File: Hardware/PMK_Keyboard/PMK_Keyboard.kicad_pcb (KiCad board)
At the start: 2 copper layers, 172 x 152 mm, 52 parts, among them IC1 SN74HC165PWR, IC2 SN74HC165PWR, IC3 SN74HC165PWR, IC4 SN74HC165PWR, IC5 SN74HC165PWR, IC7 ESP32-S2FH4, SW1 SW_Push, SW10 SW_Push, SW11 SW_Push, SW12 SW_Push, SW13 SW_Push, SW14 SW_Push, SW15 SW_Push, SW16 SW_Push, SW17 SW_Push, SW18 SW_Push, SW19 SW_Push, SW2 SW_Push, SW20 SW_Push, SW21 SW_Push, SW22 SW_Push, SW23 SW_Push, SW24 SW_Push, SW25 SW_Push, SW26 SW_Push, SW27 SW_Push, SW28 SW_Push, SW29 SW_Push, SW3 SW_Push, SW30 SW_Push, SW31 SW_Push, SW32 SW_Push, SW33 SW_Push, SW34 SW_Push, SW35 SW_Push, SW36 SW_Push, SW37 SW_Push, SW38 SW_Push, SW39 SW_Push, SW4 SW_Push, SW40 SW_Push, SW5 SW_Push, SW6 SW_Push, SW7 SW_Push, SW8 SW_Push, SW9 SW_Push

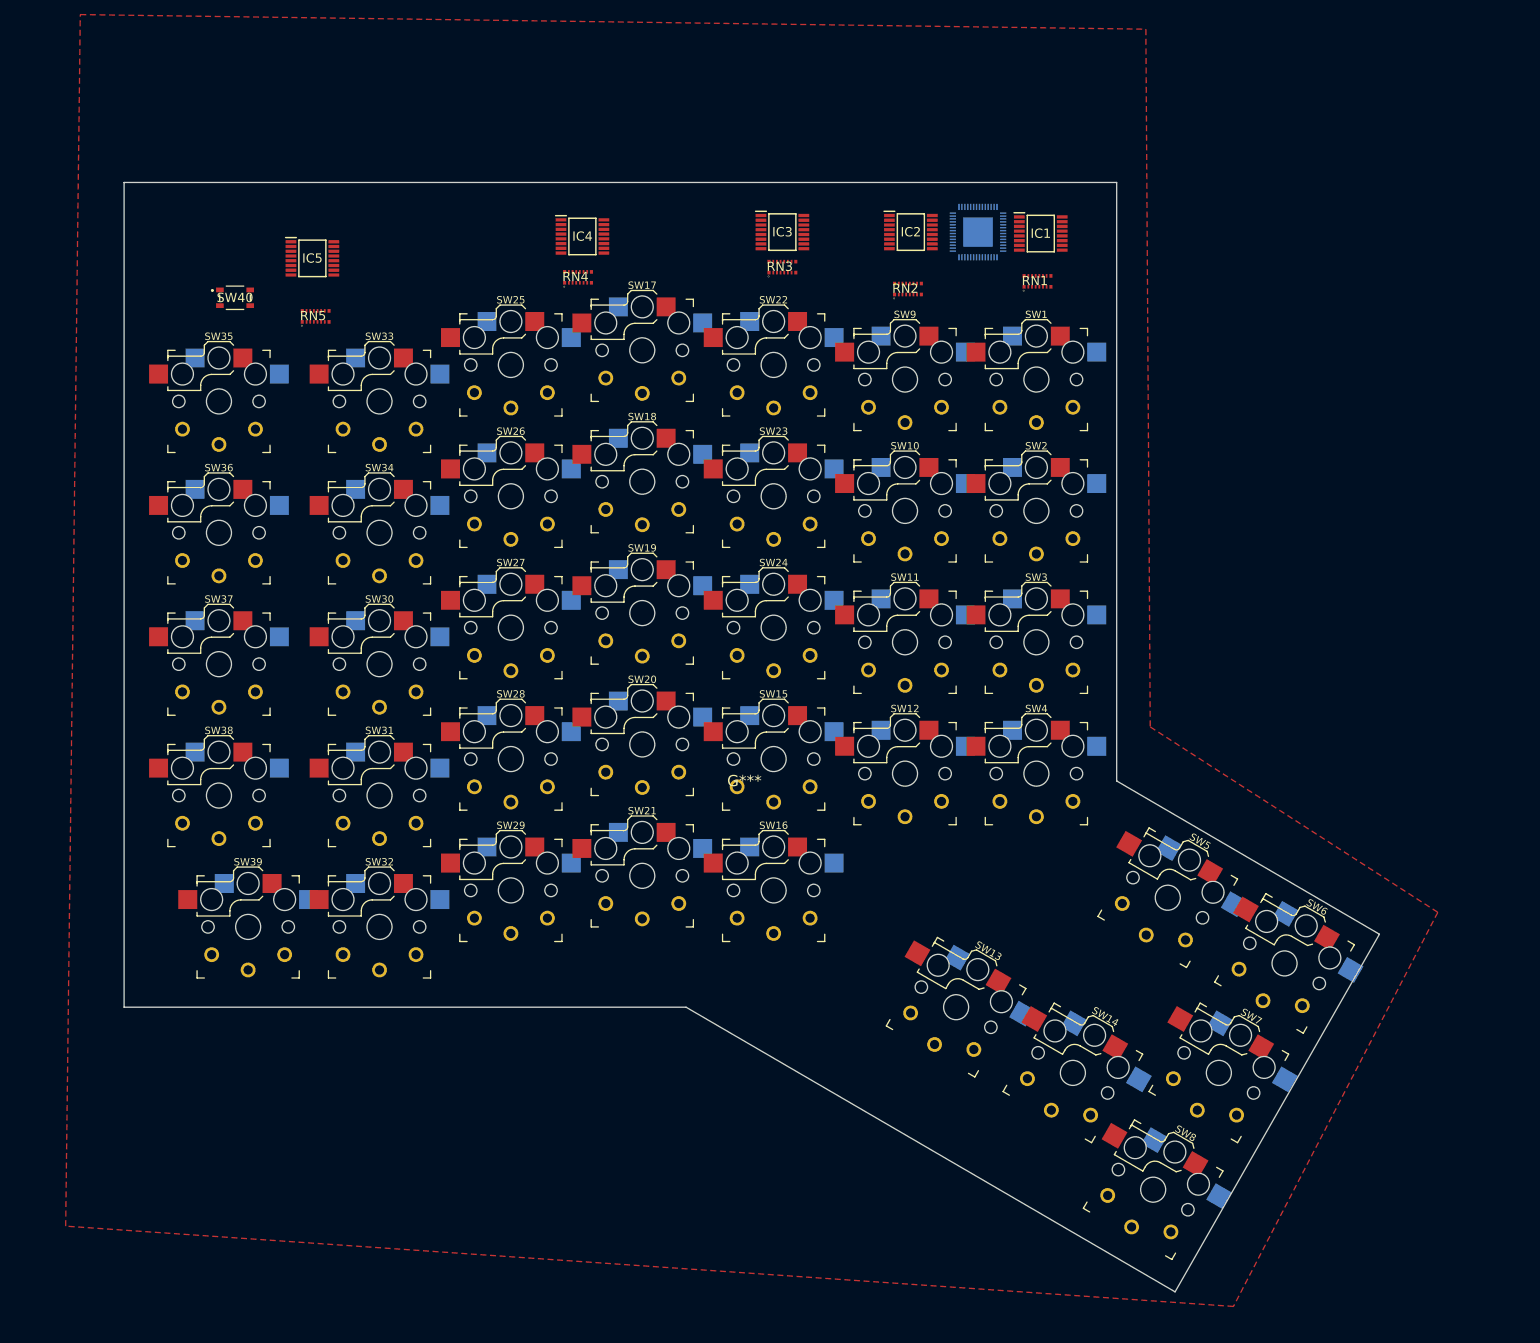
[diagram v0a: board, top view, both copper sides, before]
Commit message: changed switch footprint
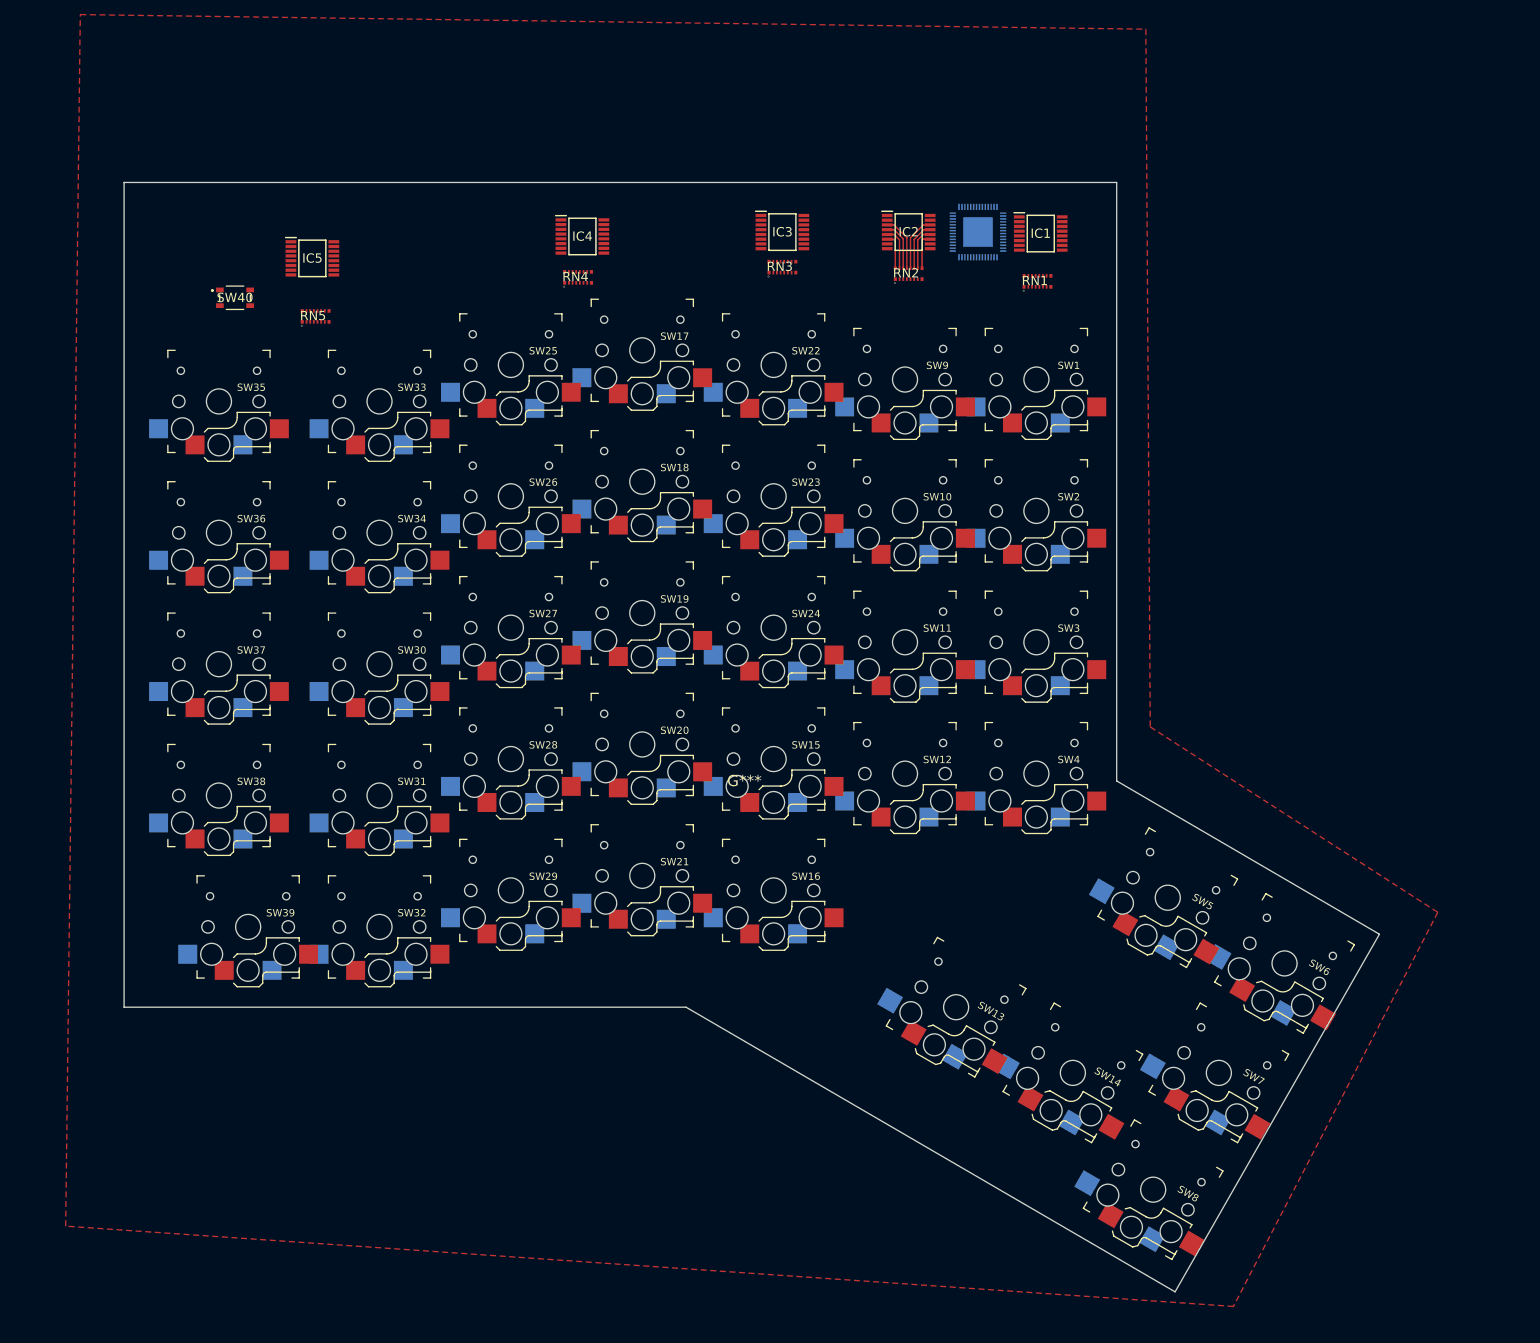
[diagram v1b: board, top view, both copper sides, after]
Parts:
- SW1, SW10, SW11, SW12, SW13, SW14, SW15, SW16, SW17, SW18, SW19, SW2, SW20, SW21, SW22, SW23, SW24, SW25, SW26, SW27, SW28, SW29, SW3, SW30, SW31, SW32, SW33, SW34, SW35, SW36, SW37, SW38, SW39, SW4, SW5, SW6, SW7, SW8, SW9: footprint Component_lib:Kailh_socket_PG1350_optional_reversible -> Component_lib:Kailh_socket_PG1350_reversible
- moved RN2 2.10 mm to (126.5, 57.5)
- moved IC2 0.30 mm to (126.5, 51.8)
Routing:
- net /12: track 0.00 -> 7.59 mm
- net /13: track 0.00 -> 7.59 mm
- net /11: track 0.00 -> 6.73 mm
- net /14: track 0.00 -> 6.68 mm
- net /10: track 0.00 -> 5.87 mm
- net /15: track 0.00 -> 5.87 mm
- net /16: track 0.00 -> 4.98 mm
- net /9: track 0.00 -> 4.91 mm

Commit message: quick routing test
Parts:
- moved RN1 0.85 mm to (145.0, 58.5)
- moved IC1 0.40 mm to (145.0, 52.0)
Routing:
- net /5: track 0.00 -> 8.47 mm
- net /4: track 0.00 -> 8.47 mm
- net /6: track 0.00 -> 7.61 mm
- net /3: track 0.00 -> 7.61 mm
- net /7: track 0.00 -> 6.75 mm
- net /2: track 0.00 -> 6.75 mm
- net /1: track 0.00 -> 5.86 mm
- net /8: track 0.00 -> 5.84 mm

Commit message: Started routing
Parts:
- IC7: moved to F.Cu
- SW40: footprint Component_lib:SKRPABE010 -> Component_lib:Kailh_socket_PG1350_reversible
- SW8: footprint Component_lib:Kailh_socket_PG1350_reversible -> Component_lib:SKRPABE010
- moved SW8 177.5 mm to (32.0, 60.0), turned to 0 degrees
- moved SW35 165.0 mm to (169.0, 167.0), turned to 150 degrees
- moved SW7 165.0 mm to (32.0, 75.0), turned to 180 degrees
- moved SW36 156.5 mm to (160.0, 183.0), turned to 150 degrees
- moved IC5 147.5 mm to (172.0, 130.0), turned to 180 degrees
- moved SW6 146.0 mm to (54.0, 75.0), turned to 180 degrees
- moved SW34 137.3 mm to (178.0, 152.0), turned to 150 degrees
- moved SW37 129.7 mm to (149.0, 167.0), turned to 150 degrees
- moved SW33 127.6 mm to (162.0, 143.0), turned to 150 degrees
- moved SW14 120.4 mm to (54.0, 93.0), turned to 180 degrees
- moved SW5 115.9 mm to (72.0, 70.0), turned to 180 degrees
- moved IC4 107.4 mm to (160.0, 126.0), turned to -90 degrees
- moved SW38 105.1 mm to (133.0, 158.0), turned to 150 degrees
- moved SW40 96.9 mm to (90.0, 140.0), turned to 180 degrees
- moved SW13 92.8 mm to (72.0, 88.0), turned to 180 degrees
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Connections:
- SW1 pad 1: GND -> /1
- SW1 pad 2: /1 -> GND
- SW10 pad 1: GND -> /10
- SW10 pad 2: /10 -> GND
- SW11 pad 1: GND -> /11
- SW11 pad 2: /11 -> GND
- SW12 pad 1: GND -> /12
- SW12 pad 2: /12 -> GND
- SW13 pad 1: GND -> /13
- SW13 pad 2: /13 -> GND
- SW14 pad 1: GND -> /14
- SW14 pad 2: /14 -> GND
- SW15 pad 1: GND -> /15
- SW15 pad 2: /15 -> GND
- SW16 pad 1: GND -> /16
- SW16 pad 2: /16 -> GND
- SW17 pad 1: GND -> /17
- SW17 pad 2: /17 -> GND
- SW18 pad 1: GND -> /18
- SW18 pad 2: /18 -> GND
- SW19 pad 1: GND -> /19
- SW19 pad 2: /19 -> GND
- SW2 pad 1: GND -> /2
- SW2 pad 2: /2 -> GND
- SW20 pad 1: GND -> /20
- SW20 pad 2: /20 -> GND
- SW21 pad 1: GND -> /21
- SW21 pad 2: /21 -> GND
- SW22 pad 1: GND -> /22
- SW22 pad 2: /22 -> GND
- SW23 pad 1: GND -> /23
- SW23 pad 2: /23 -> GND
- SW24 pad 1: GND -> /24
- SW24 pad 2: /24 -> GND
- SW25 pad 1: GND -> /25
- SW25 pad 2: /25 -> GND
- SW26 pad 1: GND -> /26
- SW26 pad 2: /26 -> GND
- SW27 pad 1: GND -> /27
- SW27 pad 2: /27 -> GND
- SW28 pad 1: GND -> /28
- SW28 pad 2: /28 -> GND
- SW29 pad 1: GND -> /29
- SW29 pad 2: /29 -> GND
- SW3 pad 1: GND -> /3
- SW3 pad 2: /3 -> GND
- SW30 pad 1: GND -> /30
- SW30 pad 2: /30 -> GND
- SW31 pad 1: GND -> /31
- SW31 pad 2: /31 -> GND
- SW32 pad 1: GND -> /32
- SW32 pad 2: /32 -> GND
- SW33 pad 1: GND -> /33
- SW33 pad 2: /33 -> GND
- SW34 pad 1: GND -> /34
- SW34 pad 2: /34 -> GND
- SW35 pad 1: GND -> /35
- SW35 pad 2: /35 -> GND
- SW36 pad 1: GND -> /36
- SW36 pad 2: /36 -> GND
- SW37 pad 1: GND -> /37
- SW37 pad 2: /37 -> GND
- SW38 pad 1: GND -> /38
- SW38 pad 2: /38 -> GND
- SW39 pad 1: GND -> /39
- SW39 pad 2: /39 -> GND
- SW4 pad 1: GND -> /4
- SW4 pad 2: /4 -> GND
- SW40 pad 1: GND -> /40
- SW40 pad 2: /40 -> GND
- SW5 pad 1: GND -> /5
- SW5 pad 2: /5 -> GND
- SW6 pad 1: GND -> /6
- SW6 pad 2: /6 -> GND
- SW7 pad 1: GND -> /7
- SW7 pad 2: /7 -> GND
- SW8 pad 1: GND -> /8
- SW8 pad 2: /8 -> GND
- SW9 pad 1: GND -> /9
- SW9 pad 2: /9 -> GND
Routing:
- net /1: track 5.86 -> 22.6 mm, vias 0 -> 1
- net /4-5: track 0.00 -> 13.5 mm
- net /36: track 0.00 -> 9.01 mm, vias 0 -> 1
- net /38: track 0.00 -> 8.58 mm, vias 0 -> 1
- net /37: track 0.00 -> 8.58 mm, vias 0 -> 1
- net /35: track 0.00 -> 8.58 mm, vias 0 -> 1
- net /34: track 0.00 -> 8.58 mm, vias 0 -> 1
- net /33: track 0.00 -> 8.58 mm, vias 0 -> 1
- net /39: track 0.00 -> 8.42 mm, vias 0 -> 1
- net /30: track 0.00 -> 8.42 mm, vias 0 -> 1
- net /32: track 0.00 -> 8.42 mm, vias 0 -> 1
- net /29: track 0.00 -> 8.42 mm, vias 0 -> 1
- net /21: track 0.00 -> 8.42 mm, vias 0 -> 1
- net /20: track 0.00 -> 8.42 mm, vias 0 -> 1
- net /19: track 0.00 -> 8.42 mm, vias 0 -> 1
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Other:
- board size 172 x 152 mm -> 174 x 153 mm

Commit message: Routing in progress
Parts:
- moved RN5 146.0 mm to (172.3, 135.2)
- moved SW33 40.0 mm to (160.0, 183.0)
- moved SW36 40.0 mm to (162.0, 143.0)
- moved SW30 36.3 mm to (36.0, 147.0)
- moved SW32 36.3 mm to (72.0, 142.0)
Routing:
- net /30: track 8.42 -> 139.6 mm
- net /31: track 8.25 -> 121.1 mm
- net /29: track 8.42 -> 106.5 mm
- net /32: track 8.42 -> 99.1 mm
- net /CLK: track 0.00 -> 90.2 mm
- net /40: track 8.25 -> 87.6 mm
- net /28: track 8.25 -> 79.4 mm
- net /33: track 8.58 -> 77.9 mm
- net /39: track 8.42 -> 68.9 mm
- net /27: track 8.25 -> 62.4 mm
- net /37: track 8.58 -> 50.4 mm
- net /38: track 8.58 -> 49.3 mm
- net /26: track 8.25 -> 43.5 mm
- net /35: track 8.58 -> 41.9 mm
- net /3-4: track 0.00 -> 21.7 mm, vias 0 -> 2
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- added copper zone on B.Cu, net GND
- removed copper zone on F.Cu, net GND

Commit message: quick routing update
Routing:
- net /33: track 77.9 -> 77.1 mm
- net /29: track 106.5 -> 105.8 mm
